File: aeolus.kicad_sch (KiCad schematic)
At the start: 42 parts, among them J1 Barrel_Jack_Switch, J2 Conn_01x04_Pin, Q1 2N3904, U1 XIAO-ESP32-C6-SMD, U2 MPM3610GQV-P, U3 LM66100DCK, U4 EMC2101-ACZL-TR, U5 INA219BIDCNR

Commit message: Inital pass at PCB
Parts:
- added C10: 0.1u, Capacitor_SMD:C_0805_2012Metric, symbol Device:C
- added C11: 10u, Capacitor_SMD:C_0805_2012Metric, symbol Device:C
- added C12: 1u, Capacitor_SMD:C_0805_2012Metric_Pad1.18x1.45mm_HandSolder, symbol Device:C
- added H1, H2: MountingHole_Pad, MountingHole:MountingHole_3.2mm_M3_Pad_Via, symbol Mechanical:MountingHole_Pad
- added J3, J4: Conn_01x04_Pin, Connector:FanPinHeader_1x04_P2.54mm_Vertical, symbol Connector:Conn_01x04_Pin
- added JP1: INA219_A0, Jumper:SolderJumper-2_P1.3mm_Open_TrianglePad1.0x1.5mm, symbol Jumper:SolderJumper_2_Open
- added JP2: INA219_A1, Jumper:SolderJumper-2_P1.3mm_Open_TrianglePad1.0x1.5mm, symbol Jumper:SolderJumper_2_Open
- added R13, R14: 10k, Resistor_SMD:R_0805_2012Metric, symbol Device:R_US
- added R15, R16: 0, Resistor_SMD:R_0805_2012Metric_Pad1.20x1.40mm_HandSolder, symbol Device:R_US
- added TP10: TACH2, TestPoint:TestPoint_Pad_D2.0mm, symbol Connector:TestPoint
- added TP9: TACH3, TestPoint:TestPoint_Pad_D2.0mm, symbol Connector:TestPoint
- added U6: 74LVC3G07, Package_SO:SSOP-8_2.95x2.8mm_P0.65mm, symbol 74xGxx:74LVC3G07
- U1: footprint OPL_Kicad_Library:XIAO-ESP32C6-SMD -> Aeolus:XIAO-ESP32C6-SMD
- U5: value INA219BIDCNR -> INA219BIDR; footprint Package_TO_SOT_SMD:SOT-23-8 -> Package_SO:SOIC-8_3.9x4.9mm_P1.27mm
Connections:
- net +3V3: now also C10.1, C11.1, JP1.2 (B), JP2.2 (B), U6.8 (VCC)
- net FAN: now also U6.1, U6.3, U6.6; no longer J2.4 (Pin_4)
- net GND: now also C10.2, C11.2, H1.1, H2.1, J3.1 (Pin_1), J4.1 (Pin_1), R13.2, R14.2, U6.4 (GND); no longer U5.7 (A0), U5.8 (A1)
- net VDC: now also J3.2 (Pin_2), J4.2 (Pin_2)
- net VSense+: now also R15.1; no longer U5.1 (VIN+)
- net VSense-: now also R16.1; no longer U5.2 (VIN-)
- net TACH2: now reaches U1.10 (GPIO20_D9_MISO)
- net TACH2: now also J3.3 (Pin_3), TP10.1
- net TACH3: now reaches U1.9 (GPIO19_D8_SCK)
- net TACH3: now also J4.3 (Pin_3), TP9.1
- net TACH renamed TACH1
- new net: JP1.1 (A), R14.1, U5.7 (A0)
- new net: JP2.1 (A), R13.1, U5.8 (A1)
- new net: C12.1, R15.2, U5.1 (VIN+)
- new net: C12.2, R16.2, U5.2 (VIN-)
- new net FAN1: J2.4 (Pin_4), U6.5
- new net FAN2: J3.4 (Pin_4), U6.2
- new net FAN3: J4.4 (Pin_4), U6.7
- no-connect marks 21 -> 19
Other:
- moved on the sheet: C5, R6, R7, R9, TP4, TP5, TP6, U1, U5

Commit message: Migrate to 4 layer board and beef up fan power distribution
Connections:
- net +12V: now also D1.2 (A2)
- net DC_IN: no longer D1.2 (A2)
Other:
- moved on the sheet: D1, F1
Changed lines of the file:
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@@
 	)
 	(junction
+		(at 67.31 41.91)
+		(diameter 0)
+		(color 0 0 0 0)
+	)
+	(junction
 		(at 158.75 251.46)
 		(diameter 0)
@@
 	)
 	(junction
-		(at 55.88 41.91)
-		(diameter 0)
-		(color 0 0 0 0)
-	)
-	(junction
 		(at 99.06 214.63)
 		(diameter 0)
@@
 	(wire
 		(pts
-			(xy 55.88 41.91) (xy 59.69 41.91)
-		)
-		(stroke
-			(width 0)
-			(type default)
-		)
-	)
-	(wire
-		(pts
 			(xy 236.22 46.99) (xy 236.22 49.53)
 		)
@@
 	(wire
 		(pts
-			(xy 55.88 41.91) (xy 55.88 43.18)
+			(xy 67.31 41.91) (xy 67.31 43.18)
 		)
 		(stroke
@@
 	(wire
 		(pts
-			(xy 67.31 41.91) (xy 73.66 41.91)
+			(xy 62.23 41.91) (xy 67.31 41.91)
 		)
 		(stroke
@@
 	(wire
 		(pts
-			(xy 45.72 41.91) (xy 55.88 41.91)
+			(xy 45.72 41.91) (xy 54.61 41.91)
 		)
 		(stroke
@@
 	(wire
 		(pts
+			(xy 67.31 41.91) (xy 73.66 41.91)
+		)
+		(stroke
+			(width 0)
+			(type default)
+		)
+	)
+	(wire
+		(pts
 			(xy 106.68 57.15) (xy 106.68 58.42)
 		)
@@
 	(wire
 		(pts
-			(xy 55.88 50.8) (xy 55.88 52.07)
+			(xy 67.31 50.8) (xy 67.31 52.07)
 		)
 		(stroke
@@
 	(symbol
 		(lib_id "power:GND")
-		(at 55.88 52.07 0)
+		(at 67.31 52.07 0)
 		(unit 1)
 		(exclude_from_sim no)
@@
 		(fields_autoplaced yes)
 		(property "Reference" "#PWR027"
-			(at 55.88 58.42 0)
+			(at 67.31 58.42 0)
 			(effects
 				(font
@@
 		)
 		(property "Value" "GND"
-			(at 55.88 57.15 0)
+			(at 67.31 57.15 0)
 			(effects
 				(font
@@
 		)
 		(property "Footprint" ""
-			(at 55.88 52.07 0)
+			(at 67.31 52.07 0)
 			(effects
 				(font
@@
 		)
 		(property "Datasheet" ""
-			(at 55.88 52.07 0)
+			(at 67.31 52.07 0)
 			(effects
 				(font
@@
 		)
 		(property "Description" "Power symbol creates a global label with name \"GND\" , ground"
-			(at 55.88 52.07 0)
+			(at 67.31 52.07 0)
 			(effects
 				(font
@@
 	(symbol
 		(lib_id "Device:Polyfuse")
-		(at 63.5 41.91 90)
+		(at 58.42 41.91 90)
 		(unit 1)
 		(exclude_from_sim no)
@@
 		(fields_autoplaced yes)
 		(property "Reference" "F1"
-			(at 63.5 35.56 90)
+			(at 58.42 35.56 90)
 			(effects
 				(font
@@
 		)
 		(property "Value" "2920L400/15MR"
-			(at 63.5 38.1 90)
+			(at 58.42 38.1 90)
 			(effects
 				(font
@@
 		)
 		(property "Footprint" "Fuse:Fuse_2920_7451Metric"
-			(at 68.58 40.64 0)
+			(at 63.5 40.64 0)
 			(effects
 				(font
@@
 		)
 		(property "Datasheet" "~"
-			(at 63.5 41.91 0)
+			(at 58.42 41.91 0)
 			(effects
 				(font
@@
 		)
 		(property "Description" "Resettable fuse, polymeric positive temperature coefficient"
-			(at 63.5 41.91 0)
+			(at 58.42 41.91 0)
 			(effects
 				(font
@@
 	(symbol
 		(lib_id "Device:D_TVS")
-		(at 55.88 46.99 90)
+		(at 67.31 46.99 90)
 		(unit 1)
 		(exclude_from_sim no)
@@
 		(fields_autoplaced yes)
 		(property "Reference" "D1"
-			(at 58.42 45.7199 90)
+			(at 64.77 45.7199 90)
 			(effects
 				(font
 					(size 1.27 1.27)
 				)
-				(justify right)
+				(justify left)
 			)
 		)
 		(property "Value" "P6SMB16A"
-			(at 58.42 48.2599 90)
+			(at 64.77 48.2599 90)
 			(effects
 				(font
 					(size 1.27 1.27)
 				)
-				(justify right)
+				(justify left)
 			)
 		)
 		(property "Footprint" "Diode_SMD:D_SMB"
-			(at 55.88 46.99 0)
+			(at 67.31 46.99 0)
 			(effects
 				(font
@@
 		)
 		(property "Datasheet" "~"
-			(at 55.88 46.99 0)
+			(at 67.31 46.99 0)
 			(effects
 				(font
@@
 		)
 		(property "Description" "Bidirectional transient-voltage-suppression diode"
-			(at 55.88 46.99 0)
+			(at 67.31 46.99 0)
 			(effects
 				(font

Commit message: feat(bom): create production files
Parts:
- C1, C11, C3, C4, C6, C7: MPN (none) -> CL21A106KAYNNNE
- C10, C8, C9: MPN (none) -> CL21B104KBCNNNC
- C12: MPN (none) -> CL21B105KBFNNNE
- C2, C5: MPN (none) -> CL21A226MAYNNNE
- D1: MPN (none) -> P6SMB16A
- D2: MPN (none) -> 15-21SYGC/S530-E2/3T
- D3: MPN (none) -> 15-21SURC/S530-A3/3T
- D4: MPN (none) -> 15-21/GHC-XS1T1/3T
- F1: MPN (none) -> 2920L400/15MR
- J1: MPN (none) -> 54-00166; now not fitted
- J2, J3, J4: MPN (none) -> 470531000; now not fitted
- Q1: MPN (none) -> 2N3904; now not fitted
- R1: MPN (none) -> RC0805FR-0753K6L
- R10, R11, R12, R13, R14, R5, R6, R7, R8: MPN (none) -> CRCW080510K0FKEAC
- R15, R16: MPN (none) -> RM10J000CT
- R2, R4: MPN (none) -> RC0805FR-07100KL
- R3: MPN (none) -> RC0805FR-0719K1L
- R9: MPN (none) -> CMS-R050-1.0
- U1: MPN (none) -> 113991254
- U2: MPN (none) -> MPM3610GQV-P
- U3: MPN (none) -> LM66100DCKR
- U4: MPN (none) -> EMC2101-ACZL-TR
- U5: MPN (none) -> INA219BIDR
- U6: MPN (none) -> 74LVC3G07SS8-7

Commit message: fix(barrel jack): Fixed the fact that it was the wrong way around
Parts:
- C1, C11, C3, C4, C6, C7: LCSC (none) -> C15850; Manufacturer Part Number (none) -> CL21A106KAYNNNE
- C10, C8, C9: LCSC (none) -> C5137467; Manufacturer Part Number (none) -> CL21B104KBCNNNC
- C12: LCSC (none) -> C5137467; Manufacturer Part Number (none) -> CL21B105KBFNNNE
- C2, C5: LCSC (none) -> C602037; Manufacturer Part Number (none) -> CL21A226MAYNNNE
- D1: LCSC (none) -> C286252; Manufacturer Part Number (none) -> P6SMB16A
- D2: LCSC (none) -> C2985981; Manufacturer Part Number (none) -> 15-21SYGC/S530-E2/3T
- D3: LCSC (none) -> C2984265; Manufacturer Part Number (none) -> 15-21SURC/S530-A3/3T
- D4: LCSC (none) -> C2984261; Manufacturer Part Number (none) -> 15-21/GHC-XS1T1/3T
- F1: value 2920L400/15MR -> 0ZCF0400FF2A; footprint Fuse:Fuse_2920_7451Metric -> Aeolus:Fuse_2920_7451Metric; MPN 2920L400/15MR -> 0ZCF0400FF2A
- J1: footprint Connector_BarrelJack:BarrelJack_Wuerth_6941xx301002 -> Aeolus:BarrelJack_Wuerth_6941xx301002
- J2, J3, J4: Manufacturer Part Number (none) -> 470531000
- Q1: Manufacturer Part Number (none) -> 2N3904
- R1: LCSC (none) -> C5153984; Manufacturer Part Number (none) -> RC0805FR-0753K6L
- R10, R11, R12, R13, R14, R5, R6, R7, R8: LCSC (none) -> C84376; Manufacturer Part Number (none) -> CRCW080510K0FKEAC
- R15, R16: LCSC (none) -> C17477; Manufacturer Part Number (none) -> RM10J000CT
- R2, R4: LCSC (none) -> C96346; Manufacturer Part Number (none) -> RC0805FR-07100KL
- R3: LCSC (none) -> C2930175; Manufacturer Part Number (none) -> RC0805FR-0719K1L
- R9: LCSC (none) -> C500733; Manufacturer Part Number (none) -> CMS-R050-1.0
- TP1, TP10, TP2, TP3, TP4, TP5, TP6, TP7, TP8, TP9: now left out of the parts list
- U1: LCSC (none) -> C9900124963; Manufacturer Part Number (none) -> 113991254
- U2: LCSC (none) -> C5183856; Manufacturer Part Number (none) -> MPM3610GQV-P
- U3: LCSC (none) -> C2832141; Manufacturer Part Number (none) -> LM66100DCKR
- U4: LCSC (none) -> C626967; Manufacturer Part Number (none) -> EMC2101-ACZL-TR
- U5: LCSC (none) -> C2155799; Manufacturer Part Number (none) -> INA219BIDR
- U6: LCSC (none) -> C2871847; Manufacturer Part Number (none) -> 74LVC3G07SS8-7

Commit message: refactor: tweak design to be better for manufacturing
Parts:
- D2: MPN 15-21SYGC/S530-E2/3T -> LTST-C150KSKT; Manufacturer Part Number 15-21SYGC/S530-E2/3T -> LTST-C150KSKT
- D3: MPN 15-21SURC/S530-A3/3T -> LTST-C150KRKT; Manufacturer Part Number 15-21SURC/S530-A3/3T -> LTST-C150KRKT
- D4: MPN 15-21/GHC-XS1T1/3T -> LTST-C150KGKT; Manufacturer Part Number 15-21/GHC-XS1T1/3T -> LTST-C150KGKT
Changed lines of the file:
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@@
 			)
 		)
-		(property "MPN" "15-21SYGC/S530-E2/3T"
+		(property "MPN" "LTST-C150KSKT"
 			(at 27.94 80.01 90)
 			(effects
@@
 			)
 		)
-		(property "Manufacturer Part Number" "15-21SYGC/S530-E2/3T"
+		(property "Manufacturer Part Number" "LTST-C150KSKT"
 			(at 27.94 80.01 0)
 			(effects
@@
 			)
 		)
-		(property "MPN" "15-21SURC/S530-A3/3T"
+		(property "MPN" "LTST-C150KRKT"
 			(at 179.07 71.12 90)
 			(effects
@@
 			)
 		)
-		(property "Manufacturer Part Number" "15-21SURC/S530-A3/3T"
+		(property "Manufacturer Part Number" "LTST-C150KRKT"
 			(at 179.07 71.12 0)
 			(effects
@@
 			)
 		)
-		(property "MPN" "15-21/GHC-XS1T1/3T"
+		(property "MPN" "LTST-C150KGKT"
 			(at 252.73 71.12 90)
 			(effects
@@
 			)
 		)
-		(property "Manufacturer Part Number" "15-21/GHC-XS1T1/3T"
+		(property "Manufacturer Part Number" "LTST-C150KGKT"
 			(at 252.73 71.12 0)
 			(effects

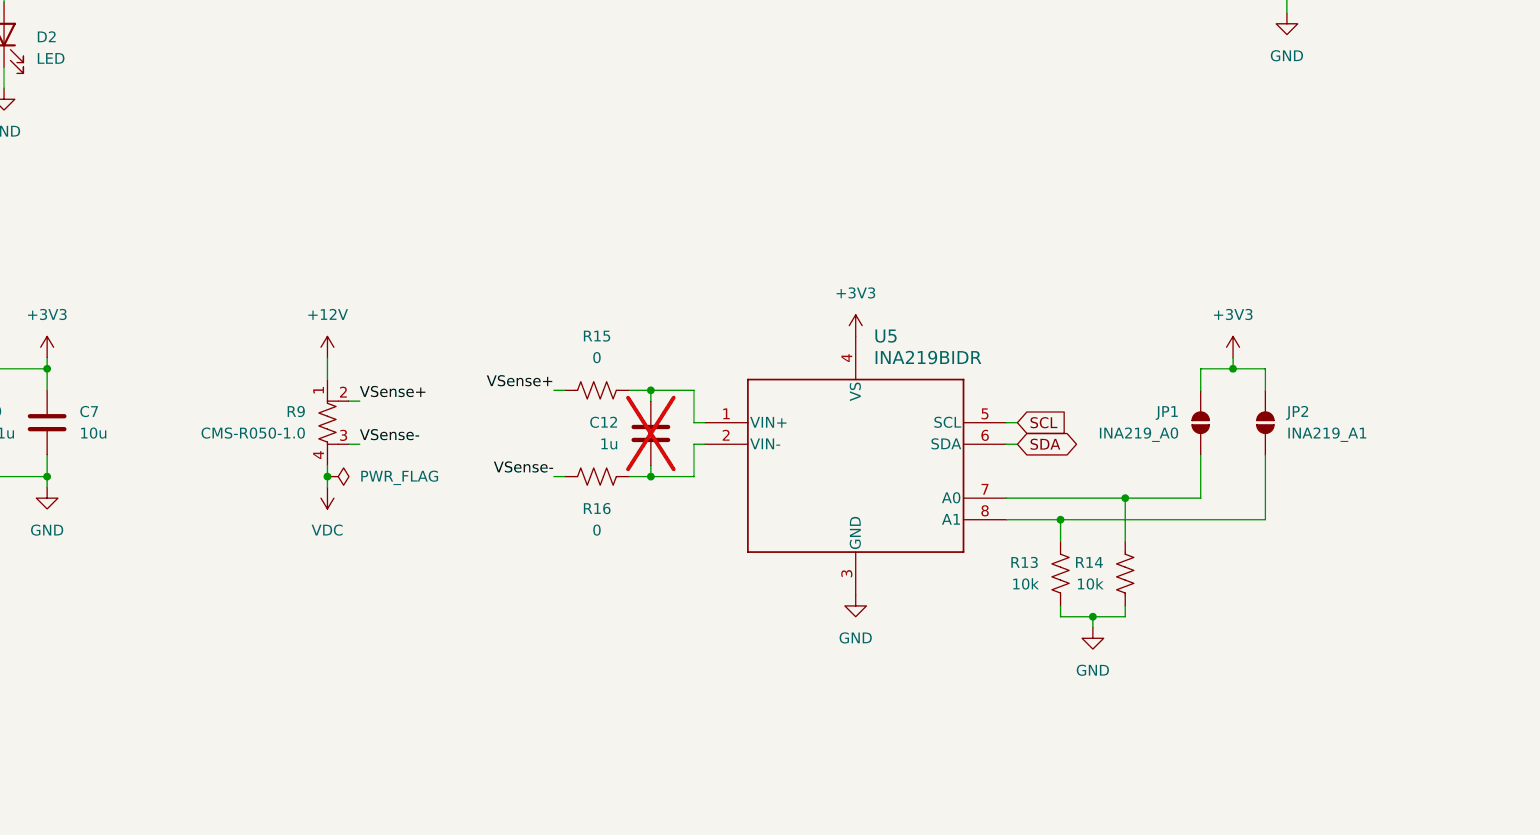
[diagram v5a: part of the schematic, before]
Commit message: refactor: use ina238 rather than ina219
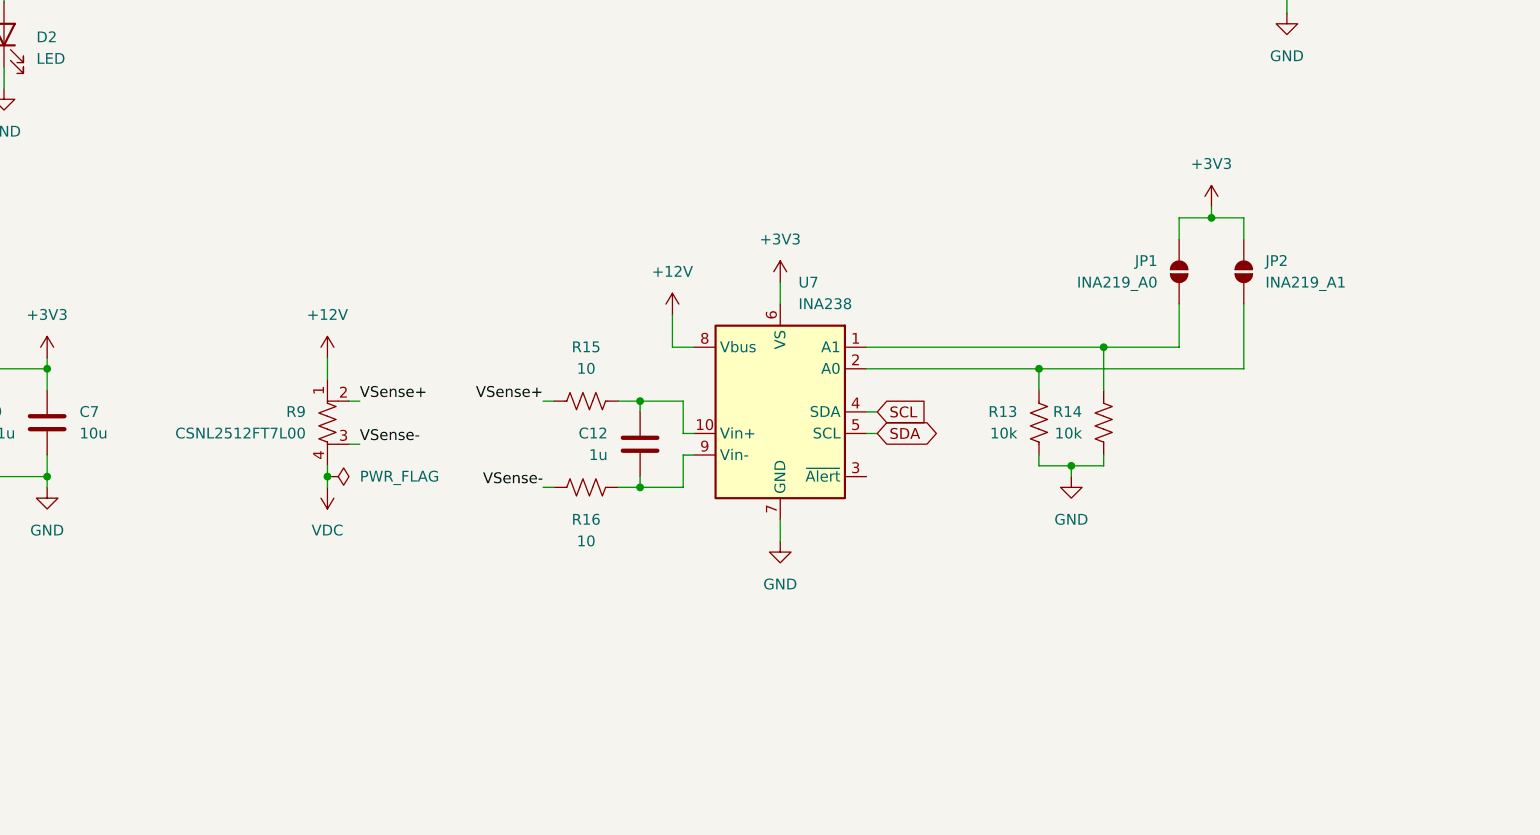
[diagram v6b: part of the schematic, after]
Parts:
- removed U5: INA219BIDR, Package_SO:SOIC-8_3.9x4.9mm_P1.27mm, symbol INA219B:INA219BIDCNR
- added U7: INA238, Package_SO:VSSOP-10_3x3mm_P0.5mm, symbol Sensor_Energy:INA238
- C12: now fitted
- J1: MPN 54-00166 -> PJ-002AH
- R15, R16: value 0 -> 10
- R9: value CMS-R050-1.0 -> CSNL2512FT7L00; footprint Resistor_SMD:R_Shunt_Vishay_WSK2512_6332Metric_T1.19mm -> Aeolus:Stackpole_Shunt_2512_Kelvin_7mOhm
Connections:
- net +12V: now also U7.8 (Vbus)
- net +3V3: now also U7.6 (VS)
- net GND: now also U7.7 (GND)
- net SCL: now also U7.4 (SDA)
- net SDA: now also U7.5 (SCL)
- net at JP1.1 (A), R14.1: now also U7.1 (A1)
- net at JP2.1 (A), R13.1: now also U7.2 (A0)
- net at C12.1, R15.2: now also U7.10 (Vin+)
- net at C12.2, R16.2: now also U7.9 (Vin-)
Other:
- moved on the sheet: JP1, JP2, R13, R14, R15, R16

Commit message: refactor: more tweaking of pcb
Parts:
- removed R12: 10k, Resistor_SMD:R_0805_2012Metric, symbol Device:R_US
- added J5, J6: Conn_01x04_Pin, symbol Connector:Conn_01x04_Pin
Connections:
- net VCC_OK: now reaches R5.2, U3.5 (ST)
- net VCC_OK: now also D4.2 (A)
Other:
- moved on the sheet: D4

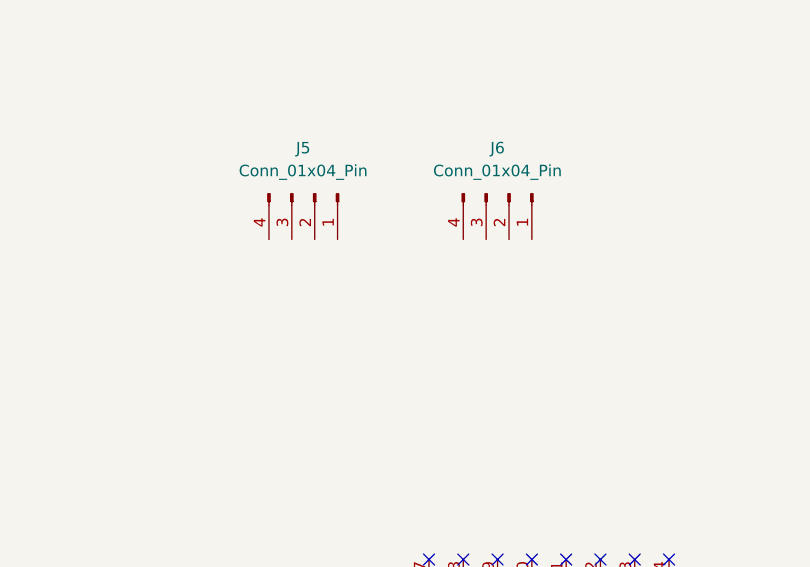
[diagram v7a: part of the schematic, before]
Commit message: feat: add qwiik connectors to board
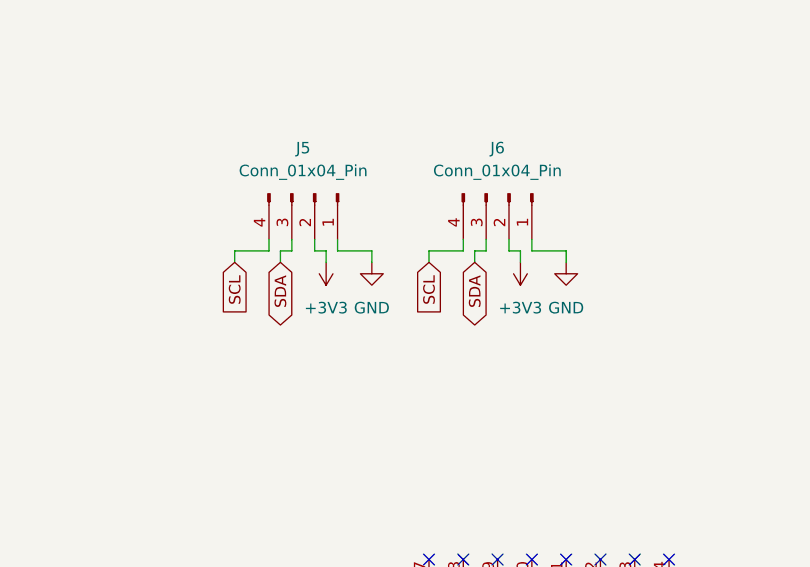
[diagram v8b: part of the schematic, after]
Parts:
- J5, J6: footprint (none) -> Aeolus:JST BM04B-SRSS-TB(LF)(SN)_4xP1.00mm
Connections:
- net +3V3: now also J5.2 (Pin_2), J6.2 (Pin_2)
- net GND: now also J5.1 (Pin_1), J6.1 (Pin_1)
- net SCL: now also J5.4 (Pin_4), J6.4 (Pin_4)
- net SDA: now also J5.3 (Pin_3), J6.3 (Pin_3)
